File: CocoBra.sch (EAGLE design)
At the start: 16 parts, among them U3 ATTINY84

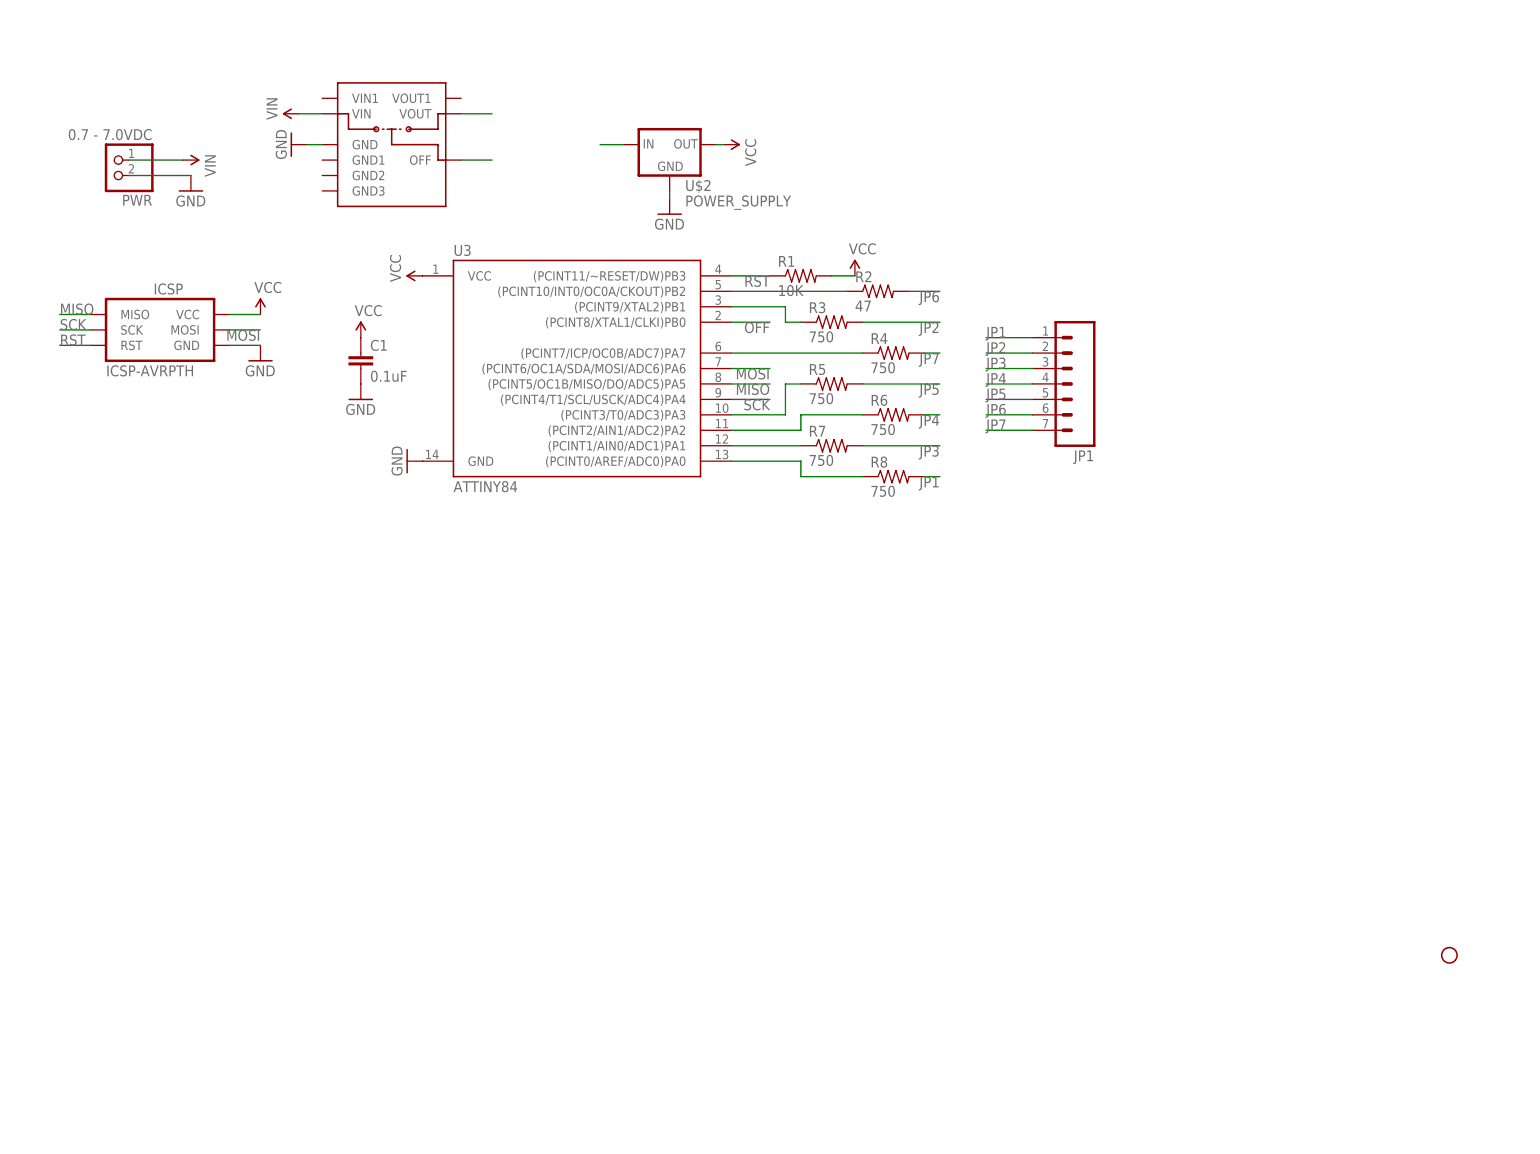
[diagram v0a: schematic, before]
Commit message: Added tilt switch. EagleUp model taking shape
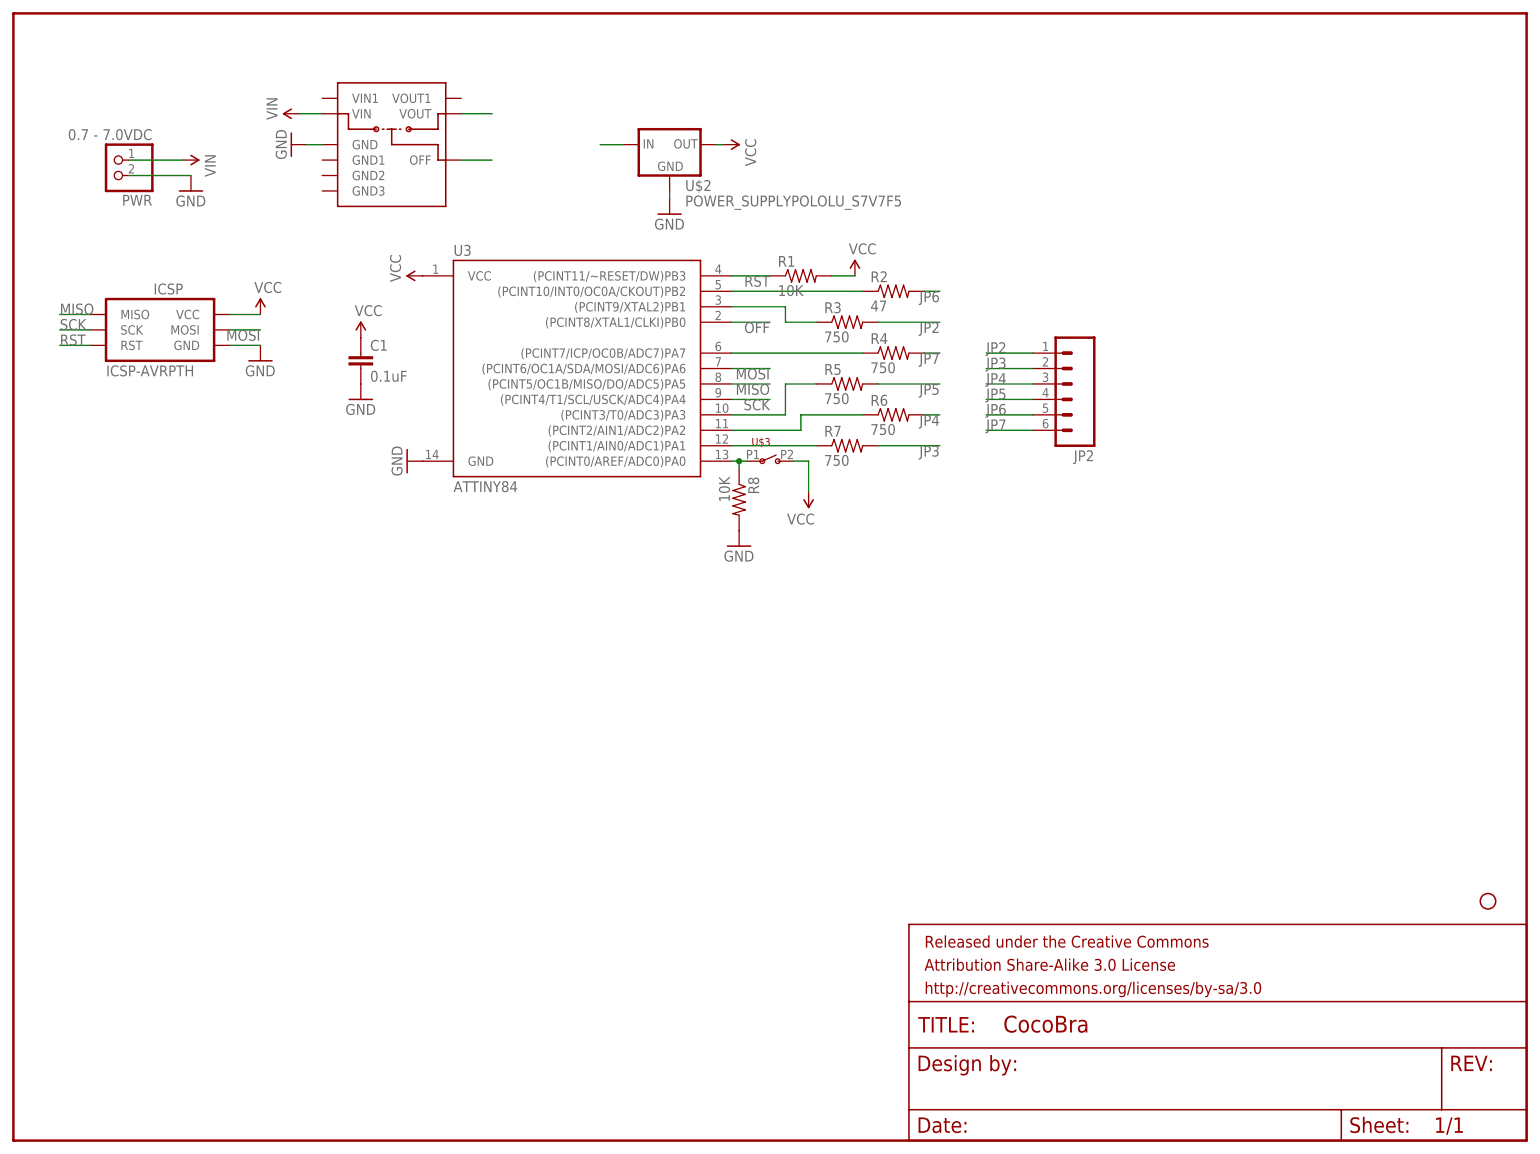
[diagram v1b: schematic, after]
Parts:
- removed JP1: (no value), SparkFun-Connectors:M07
- added FRAME1: FRAME-LETTER, SparkFun-Aesthetics:FRAME-LETTER
- added JP2: (no value), SparkFun-Connectors:M06SIP
- added U$3: SWITCH-SPSTTILT, Dek:SWITCH-SPSTTILT
- R1: device Dek:RESISTORAXIAL-0.3 -> Dek:RESISTORAXIAL-0.2
- R8: value 750 -> 10K; device Dek:RESISTORAXIAL-0.3 -> Dek:RESISTORAXIAL-0.2
- U$2: value POWER_SUPPLY -> POWER_SUPPLYPOLOLU_S7V7F5; device Dek:POWER_SUPPLY -> Dek:POWER_SUPPLYPOLOLU_S7V7F5
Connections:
- removed net JP1: JP1.1, R8.2
- net GND: now also R8.2
- net JP2: now also JP2.1; no longer JP1.2
- net JP3: now also JP2.2; no longer JP1.3
- net JP4: now also JP2.3; no longer JP1.4
- net JP5: now also JP2.4; no longer JP1.5
- net JP6: now also JP2.5; no longer JP1.6
- net JP7: now also JP2.6; no longer JP1.7
- net N$7: now also U$3.P1
- net VCC: now also U$3.P2
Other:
- moved on the sheet: R2, R3, R5, R7, R8
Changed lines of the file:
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@@
 <part name="SUPPLY7" library="SparkFun-Aesthetics" deviceset="VIN" device=""/>
 <part name="U$4" library="Dek" deviceset="POLOLU_POWER_SWITCH" device="PTH"/>
-<part name="R1" library="Dek" deviceset="RESISTOR" device="AXIAL-0.3" value="10K"/>
+<part name="R1" library="Dek" deviceset="RESISTOR" device="AXIAL-0.2" value="10K"/>
 <part name="R2" library="Dek" deviceset="RESISTOR" device="AXIAL-0.3" value="47"/>
 <part name="R3" library="Dek" deviceset="RESISTOR" device="AXIAL-0.3" value="750"/>
@@
 <part name="R6" library="Dek" deviceset="RESISTOR" device="AXIAL-0.3" value="750"/>
 <part name="R7" library="Dek" deviceset="RESISTOR" device="AXIAL-0.3" value="750"/>
-<part name="R8" library="Dek" deviceset="RESISTOR" device="AXIAL-0.3" value="750"/>
+<part name="R8" library="Dek" deviceset="RESISTOR" device="AXIAL-0.2" value="10K"/>
 <part name="SUPPLY9" library="SparkFun-Aesthetics" deviceset="VCC" device=""/>
-<part name="JP1" library="SparkFun-Connectors" deviceset="M07" device=""/>
 <part name="STANDOFF3" library="Dek" deviceset="STAND-OFF" device="#2"/>
-<part name="U$2" library="Dek" deviceset="POWER_SUPPLY" device=""/>
+<part name="U$2" library="Dek" deviceset="POWER_SUPPLY" device="POLOLU_S7V7F5"/>
+<part name="U$3" library="Dek" deviceset="SWITCH-SPST" device="TILT"/>
+<part name="GND7" library="supply1" deviceset="GND" device=""/>
+<part name="SUPPLY2" library="SparkFun-Aesthetics" deviceset="VCC" device=""/>
+<part name="FRAME1" library="SparkFun-Aesthetics" deviceset="FRAME-LETTER" device=""/>
+<part name="JP2" library="SparkFun-Connectors" deviceset="M06" device="SIP"/>
 </parts>
 <sheets>
@@
 <instance part="GND6" gate="1" x="45.72" y="163.83" rot="R270"/>
 <instance part="SUPPLY7" gate="G$1" x="46.99" y="168.91" rot="R90"/>
-<instance part="U$4" gate="G$1" x="53.34" y="161.29"/>
+<instance part="U$4" gate="G$1" x="53.34" y="153.67"/>
 <instance part="R1" gate="G$1" x="129.54" y="142.24"/>
-<instance part="R2" gate="G$1" x="142.24" y="139.7"/>
-<instance part="R3" gate="G$1" x="134.62" y="134.62"/>
+<instance part="R2" gate="G$1" x="144.78" y="139.7"/>
+<instance part="R3" gate="G$1" x="137.16" y="134.62"/>
 <instance part="R4" gate="G$1" x="144.78" y="129.54"/>
-<instance part="R5" gate="G$1" x="134.62" y="124.46"/>
+<instance part="R5" gate="G$1" x="137.16" y="124.46"/>
 <instance part="R6" gate="G$1" x="144.78" y="119.38"/>
-<instance part="R7" gate="G$1" x="134.62" y="114.3"/>
-<instance part="R8" gate="G$1" x="144.78" y="109.22"/>
+<instance part="R7" gate="G$1" x="137.16" y="114.3"/>
+<instance part="R8" gate="G$1" x="119.38" y="105.41" rot="R270"/>
 <instance part="SUPPLY9" gate="1" x="138.43" y="142.24"/>
-<instance part="JP1" gate="G$1" x="172.72" y="127" rot="R180"/>
-<instance part="STANDOFF3" gate="G$1" x="236.22" y="30.48"/>
+<instance part="STANDOFF3" gate="G$1" x="242.57" y="39.37"/>
 <instance part="U$2" gate="G$1" x="107.95" y="163.83"/>
+<instance part="U$3" gate="G$1" x="125.73" y="111.76"/>
+<instance part="GND7" gate="1" x="119.38" y="97.79"/>
+<instance part="SUPPLY2" gate="1" x="130.81" y="106.68" rot="R180"/>
+<instance part="FRAME1" gate="G$1" x="0" y="0"/>
+<instance part="FRAME1" gate="G$2" x="147.32" y="0"/>
+<instance part="JP2" gate="G$1" x="172.72" y="124.46" rot="R180"/>
 </instances>
 <busses>
@@
 <pinref part="U$4" gate="G$1" pin="GND"/>
 </segment>
+<segment>
+<pinref part="R8" gate="G$1" pin="2"/>
+<pinref part="GND7" gate="1" pin="GND"/>
+</segment>
 </net>
 <net name="VIN" class="1">
@@
 <pinref part="SUPPLY9" gate="1" pin="VCC"/>
 <wire x1="138.43" y1="142.24" x2="134.62" y2="142.24" width="0.1524" layer="91"/>
+</segment>
+<segment>
+<pinref part="U$3" gate="G$1" pin="P2"/>
+<pinref part="SUPPLY2" gate="1" pin="VCC"/>
+<wire x1="130.81" y1="106.68" x2="130.81" y2="111.76" width="0.1524" layer="91"/>
+<wire x1="130.81" y1="111.76" x2="128.27" y2="111.76" width="0.1524" layer="91"/>
 </segment>
 </net>
@@
 <pinref part="U3" gate="G$1" pin="(PCINT10/INT0/OC0A/CKOUT)PB2"/>
 <pinref part="R2" gate="G$1" pin="1"/>
-<wire x1="137.16" y1="139.7" x2="118.11" y2="139.7" width="0.1524" layer="91"/>
+<wire x1="139.7" y1="139.7" x2="118.11" y2="139.7" width="0.1524" layer="91"/>
 </segment>
 </net>
@@
 <pinref part="U3" gate="G$1" pin="(PCINT9/XTAL2)PB1"/>
 <pinref part="R3" gate="G$1" pin="1"/>
-<wire x1="129.54" y1="134.62" x2="127" y2="134.62" width="0.1524" layer="91"/>
+<wire x1="132.08" y1="134.62" x2="127" y2="134.62" width="0.1524" layer="91"/>
 <wire x1="127" y1="134.62" x2="127" y2="137.16" width="0.1524" layer="91"/>
 <wire x1="127" y1="137.16" x2="118.11" y2="137.16" width="0.1524" layer="91"/>
@@
 <pinref part="U3" gate="G$1" pin="(PCINT3/T0/ADC3)PA3"/>
 <pinref part="R5" gate="G$1" pin="1"/>
-<wire x1="129.54" y1="124.46" x2="127" y2="124.46" width="0.1524" layer="91"/>
+<wire x1="132.08" y1="124.46" x2="127" y2="124.46" width="0.1524" layer="91"/>
 <wire x1="127" y1="124.46" x2="127" y2="119.38" width="0.1524" layer="91"/>
 <wire x1="127" y1="119.38" x2="118.11" y2="119.38" width="0.1524" layer="91"/>
@@
 <pinref part="U3" gate="G$1" pin="(PCINT1/AIN0/ADC1)PA1"/>
 <pinref part="R7" gate="G$1" pin="1"/>
-<wire x1="129.54" y1="114.3" x2="118.11" y2="114.3" width="0.1524" layer="91"/>
-</segment>
-</net>
-<net name="N$7" class="0">
-<segment>
-<pinref part="U3" gate="G$1" pin="(PCINT0/AREF/ADC0)PA0"/>
-<pinref part="R8" gate="G$1" pin="1"/>
-<wire x1="139.7" y1="109.22" x2="129.54" y2="109.22" width="0.1524" layer="91"/>
-<wire x1="129.54" y1="109.22" x2="129.54" y2="111.76" width="0.1524" layer="91"/>
-<wire x1="129.54" y1="111.76" x2="118.11" y2="111.76" width="0.1524" layer="91"/>
-</segment>
-</net>
-<net name="JP1" class="0">
-<segment>
-<wire x1="167.64" y1="132.08" x2="160.02" y2="132.08" width="0.1524" layer="91"/>
-<pinref part="JP1" gate="G$1" pin="1"/>
-<label x="160.02" y="132.08" size="1.778" layer="95"/>
-</segment>
-<segment>
-<wire x1="149.86" y1="109.22" x2="152.4" y2="109.22" width="0.1524" layer="91"/>
-<pinref part="R8" gate="G$1" pin="2"/>
-<label x="152.4" y="109.22" size="1.778" layer="95" rot="R180"/>
+<wire x1="132.08" y1="114.3" x2="118.11" y2="114.3" width="0.1524" layer="91"/>
 </segment>
 </net>
 <net name="JP2" class="0">
 <segment>
-<pinref part="JP1" gate="G$1" pin="2"/>
 <wire x1="167.64" y1="129.54" x2="160.02" y2="129.54" width="0.1524" layer="91"/>
 <label x="160.02" y="129.54" size="1.778" layer="95"/>
+<pinref part="JP2" gate="G$1" pin="1"/>
 </segment>
 <segment>
 <pinref part="R3" gate="G$1" pin="2"/>
-<wire x1="139.7" y1="134.62" x2="152.4" y2="134.62" width="0.1524" layer="91"/>
+<wire x1="142.24" y1="134.62" x2="152.4" y2="134.62" width="0.1524" layer="91"/>
 <label x="152.4" y="134.62" size="1.778" layer="95" rot="R180"/>
 </segment>
@@
 <net name="JP3" class="0">
 <segment>
-<pinref part="JP1" gate="G$1" pin="3"/>
 <wire x1="167.64" y1="127" x2="160.02" y2="127" width="0.1524" layer="91"/>
 <label x="160.02" y="127" size="1.778" layer="95"/>
+<pinref part="JP2" gate="G$1" pin="2"/>
 </segment>
 <segment>
 <pinref part="R7" gate="G$1" pin="2"/>
-<wire x1="139.7" y1="114.3" x2="152.4" y2="114.3" width="0.1524" layer="91"/>
+<wire x1="142.24" y1="114.3" x2="152.4" y2="114.3" width="0.1524" layer="91"/>
 <label x="152.4" y="114.3" size="1.778" layer="95" rot="R180"/>
 </segment>
@@
 <net name="JP4" class="0">
 <segment>
-<pinref part="JP1" gate="G$1" pin="4"/>
 <wire x1="167.64" y1="124.46" x2="160.02" y2="124.46" width="0.1524" layer="91"/>
 <label x="160.02" y="124.46" size="1.778" layer="95"/>
+<pinref part="JP2" gate="G$1" pin="3"/>
 </segment>
 <segment>
@@
 <net name="JP5" class="0">
 <segment>
-<pinref part="JP1" gate="G$1" pin="5"/>
 <wire x1="167.64" y1="121.92" x2="160.02" y2="121.92" width="0.1524" layer="91"/>
 <label x="160.02" y="121.92" size="1.778" layer="95"/>
+<pinref part="JP2" gate="G$1" pin="4"/>
 </segment>
 <segment>
 <pinref part="R5" gate="G$1" pin="2"/>
-<wire x1="139.7" y1="124.46" x2="152.4" y2="124.46" width="0.1524" layer="91"/>
+<wire x1="142.24" y1="124.46" x2="152.4" y2="124.46" width="0.1524" layer="91"/>
 <label x="152.4" y="124.46" size="1.778" layer="95" rot="R180"/>
 </segment>
@@
 <net name="JP6" class="0">
 <segment>
-<pinref part="JP1" gate="G$1" pin="6"/>
 <wire x1="167.64" y1="119.38" x2="160.02" y2="119.38" width="0.1524" layer="91"/>
 <label x="160.02" y="119.38" size="1.778" layer="95"/>
+<pinref part="JP2" gate="G$1" pin="5"/>
 </segment>
 <segment>
 <pinref part="R2" gate="G$1" pin="2"/>
-<wire x1="147.32" y1="139.7" x2="152.4" y2="139.7" width="0.1524" layer="91"/>
+<wire x1="149.86" y1="139.7" x2="152.4" y2="139.7" width="0.1524" layer="91"/>
 <label x="152.4" y="139.7" size="1.778" layer="95" rot="R180"/>
 </segment>
@@
 <net name="JP7" class="0">
 <segment>
-<pinref part="JP1" gate="G$1" pin="7"/>
 <wire x1="167.64" y1="116.84" x2="160.02" y2="116.84" width="0.1524" layer="91"/>
 <label x="160.02" y="116.84" size="1.778" layer="95"/>
+<pinref part="JP2" gate="G$1" pin="6"/>
 </segment>
 <segment>
@@
 </segment>
 </net>
+<net name="N$7" class="0">
+<segment>
+<pinref part="U3" gate="G$1" pin="(PCINT0/AREF/ADC0)PA0"/>
+<pinref part="U$3" gate="G$1" pin="P1"/>
+<wire x1="120.65" y1="111.76" x2="119.38" y2="111.76" width="0.1524" layer="91"/>
+<pinref part="R8" gate="G$1" pin="1"/>
+<wire x1="119.38" y1="111.76" x2="118.11" y2="111.76" width="0.1524" layer="91"/>
+<wire x1="119.38" y1="110.49" x2="119.38" y2="111.76" width="0.1524" layer="91"/>
+<junction x="119.38" y="111.76"/>
+</segment>
+</net>
